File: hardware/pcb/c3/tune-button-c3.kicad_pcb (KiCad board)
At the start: 2 copper layers, 46 x 77 mm, 39 parts, among them J1 USB-C, J2 LiPo, Q1 AO3401A, SW1 MX switch, SW2 MX switch, SW3 MX switch, SW4 MX switch, SW5 RESET, SW6 BOOT, U1 ESP32-C3-WROOM-02-N4, U2 USBLC6-2SC6, U3 MCP73831-2, U4 MCP1700-3302E

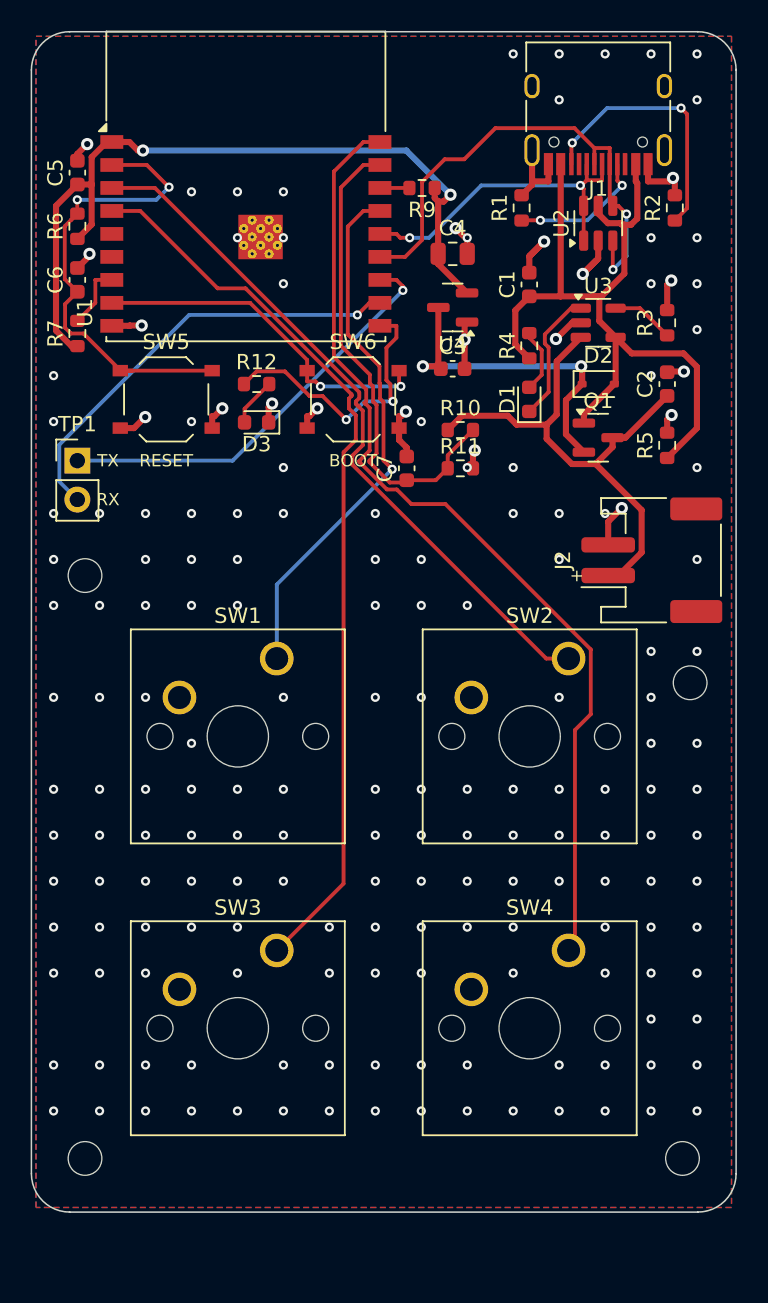
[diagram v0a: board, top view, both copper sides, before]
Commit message: PCBs: keep screw heads and labels clear of the keycaps
Mounting holes move out from under the caps (both boards 2.5 mm longer), and part labels are placed
automatically beside each part, off pads, bodies and the XIAO's outline.
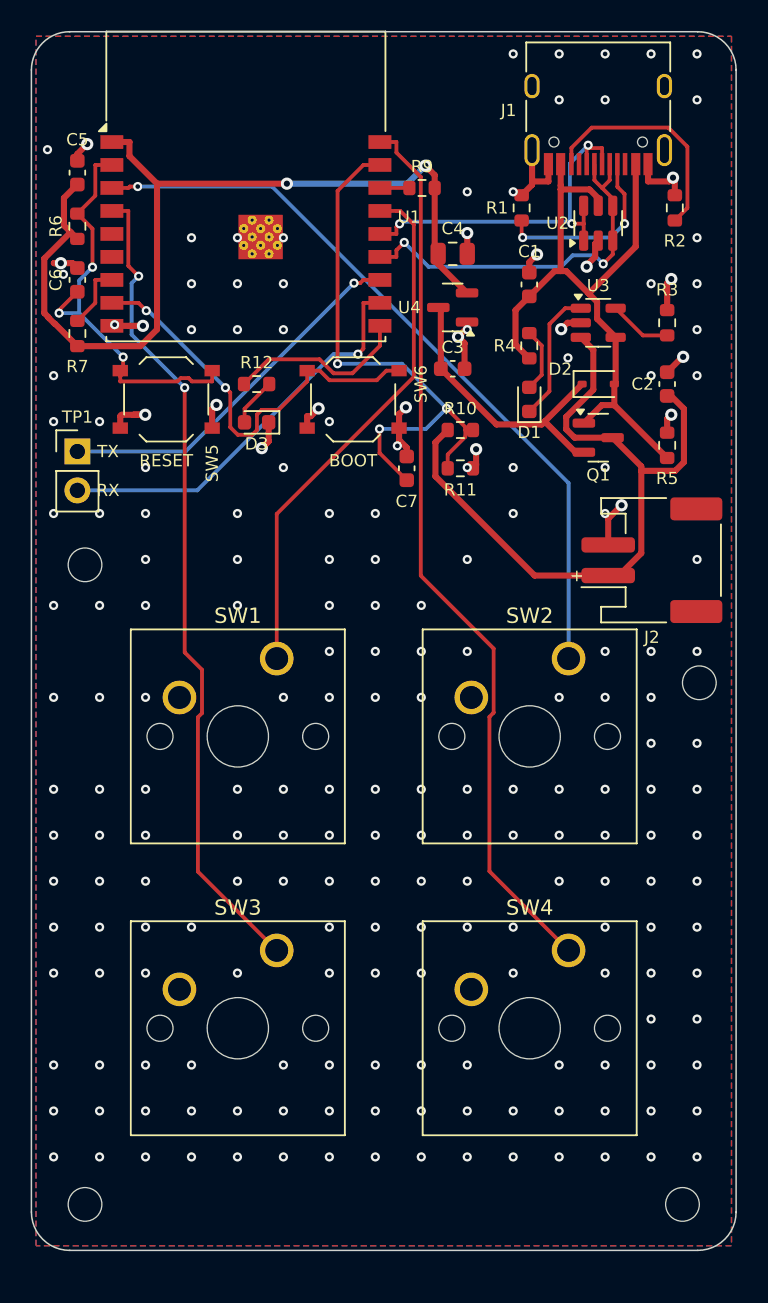
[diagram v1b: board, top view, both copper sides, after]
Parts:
- moved H1 3.00 mm to (42.5, 76.5)
- moved H2 3.00 mm to (3.50, 76.5)
- moved H3 0.70 mm to (3.50, 34.8)
- moved H4 0.60 mm to (43.6, 42.5)
- moved TP1 0.60 mm to (3.00, 27.4)
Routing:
- net VBAT: track 35.2 -> 46.7 mm
- net 3V3: track 52.6 -> 60.6 mm
- net VBUS: track 53.0 -> 45.2 mm
- net USB_DN: track 33.2 -> 25.4 mm
- net LED: track 18.3 -> 12.0 mm, vias 2 -> 0
- net VBAT_SENSE: track 31.5 -> 37.5 mm, vias 0 -> 3
- net K4: track 64.6 -> 58.7 mm
- net K3: track 59.3 -> 54.0 mm, vias 0 -> 2
- net EN: track 32.2 -> 28.1 mm, vias 2 -> 3
- net IO9: track 23.0 -> 26.9 mm
- net TXD: track 27.8 -> 24.4 mm
- net CC1: track 9.03 -> 12.2 mm
- net USB_DP: track 22.0 -> 25.0 mm, vias 2 -> 3
- net K2: track 46.6 -> 49.3 mm, vias 0 -> 1
- net VSYS: track 22.0 -> 19.3 mm, vias 2 -> 0
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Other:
- board size 46 x 77 mm -> 46 x 79.5 mm

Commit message: C3 PCB: no board under the antenna, USB-C to the bottom edge
The top-left corner is cut away under the module's antenna, as Espressif's layout guide prefers,
and USB-C moves to the middle of the bottom edge (about 70 mm from the antenna) with its ESD
part and CC resistors between the lower switches. The receptacle's face now sits 0.2 mm proud of
the edge so a plug's moulding clears the board.
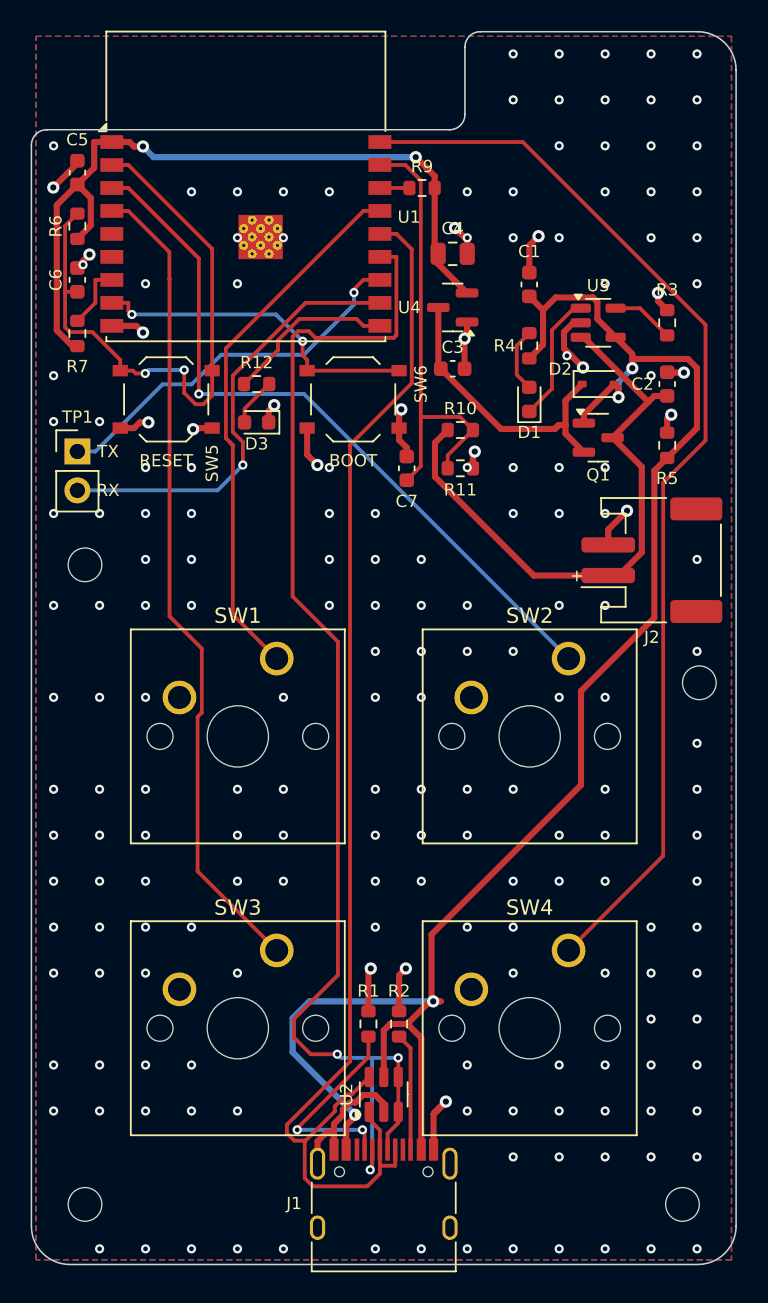
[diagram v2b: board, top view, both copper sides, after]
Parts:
- moved J1 73.8 mm to (23.0, 77.0), turned to 0 degrees
- moved U2 58.6 mm to (23.0, 69.4)
- moved R2 56.2 mm to (24.0, 64.8)
- moved R1 54.2 mm to (22.0, 64.8)
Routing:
- net VBUS: track 45.2 -> 110.0 mm, vias 0 -> 4
- net USB_DP: track 25.0 -> 85.4 mm, vias 3 -> 0
- net USB_DN: track 25.4 -> 83.9 mm, vias 2 -> 3
- net EN: track 28.1 -> 40.3 mm, vias 3 -> 2
- net K4: track 58.7 -> 70.7 mm
- net 3V3: track 60.6 -> 51.0 mm
- net GND: track 49.7 -> 57.4 mm, vias 208 -> 197
- net VBAT_SENSE: track 37.5 -> 30.0 mm, vias 3 -> 0
- net VBAT: track 46.7 -> 39.3 mm
- net CC2: track 14.9 -> 7.69 mm
- net IO9: track 26.9 -> 21.8 mm
- net RXD: track 26.6 -> 29.2 mm
- net K2: track 49.3 -> 47.7 mm
- net CC1: track 12.2 -> 13.6 mm
- net K1: track 34.6 -> 35.7 mm
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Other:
- board size 46 x 79.5 mm -> 46 x 80.5 mm

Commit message: C3 PCB: JLC Basic/Preferred parts where a drop-in exists, LCSC numbers, JLC BOM and CPL
TP4054 for MCP73831, XC6206 for MCP1700 and SRV05-4 for USBLC6-2SC6, each with the same footprint
and pinout. Every assembled part carries its LCSC number; the build writes JLC-format BOM and
placement files listing only those parts. Only the module, USB-C and JST sockets remain Extended.
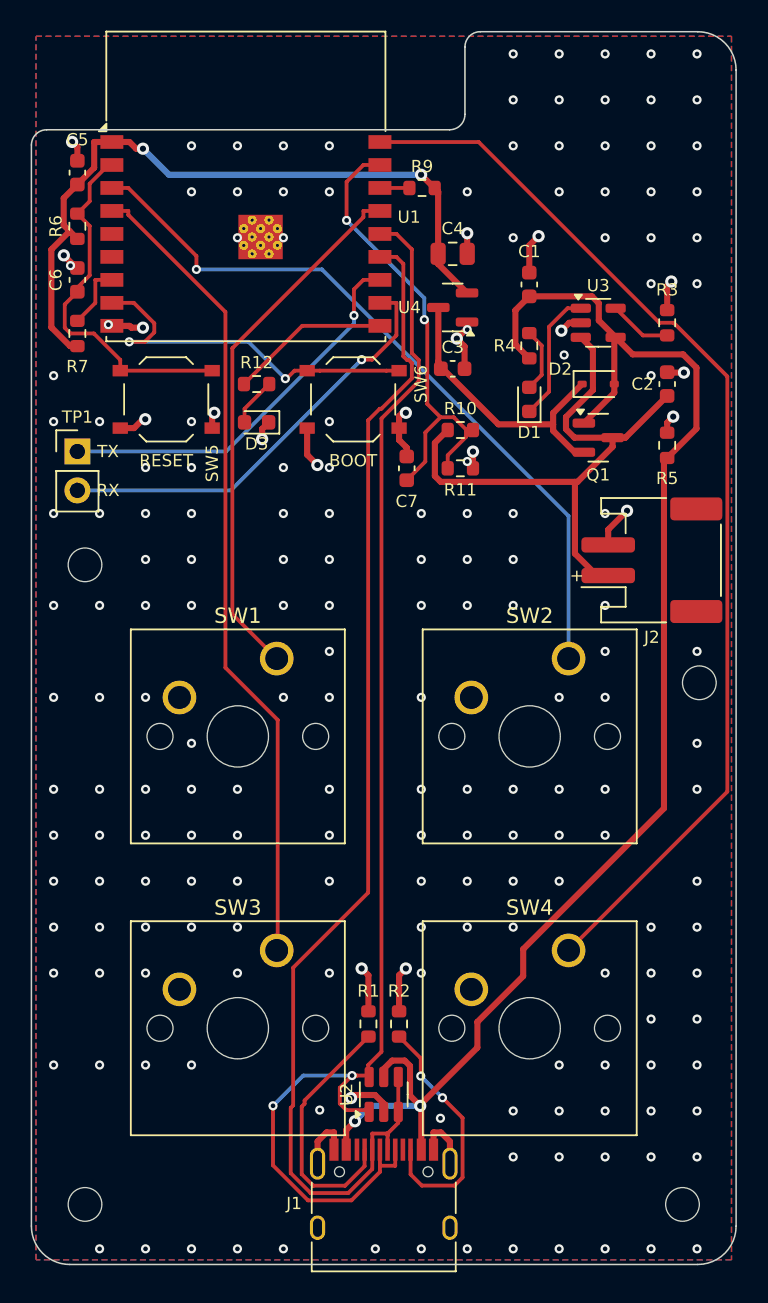
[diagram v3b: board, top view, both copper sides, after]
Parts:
- U2: value USBLC6-2SC6 -> SRV05-4
- U3: value MCP73831-2 -> TP4054
- U4: value MCP1700-3302E -> XC6206P332MR
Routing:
- net EN: track 40.3 -> 23.9 mm, vias 2 -> 0
- net VBUS: track 110.0 -> 95.6 mm, vias 4 -> 2
- net CC2: track 7.69 -> 16.4 mm, vias 0 -> 2
- net GND: track 57.4 -> 49.9 mm, vias 197 -> 199
- net USB_DN: track 83.9 -> 79.6 mm, vias 3 -> 0
- net CC1: track 13.6 -> 16.8 mm, vias 2 -> 0
- net 3V3: track 51.0 -> 48.2 mm
- net IO9: track 21.8 -> 24.6 mm
- net VBAT_SENSE: track 30.0 -> 31.0 mm, vias 0 -> 2
- net RXD: track 29.2 -> 28.2 mm
- net K2: track 47.7 -> 48.5 mm
- net LED: track 11.2 -> 10.4 mm
- net TXD: track 25.0 -> 25.7 mm
- net K1: track 35.7 -> 35.0 mm
- net USB_DP: track 85.4 -> 85.5 mm, vias 0 -> 2

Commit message: C3 PCB: switches and LEDs on the back, electronics on the front, EdgeCoil mark on the key side
The MX switches mount on the back (mirrored so K1 is still top left from the key side), and only
their leads and posts need room on the front, guarded by part-free rule areas. That lets the keys
sit behind the electronics: the board is 69.5 mm long instead of 80.5. The two LEDs move to the key
side as hand-soldered 0805s; the battery socket and UART pads sit between the key rows. The key side
carries the mark, the board name and LED labels; part labels are placed per side and kept off the
antenna notch.
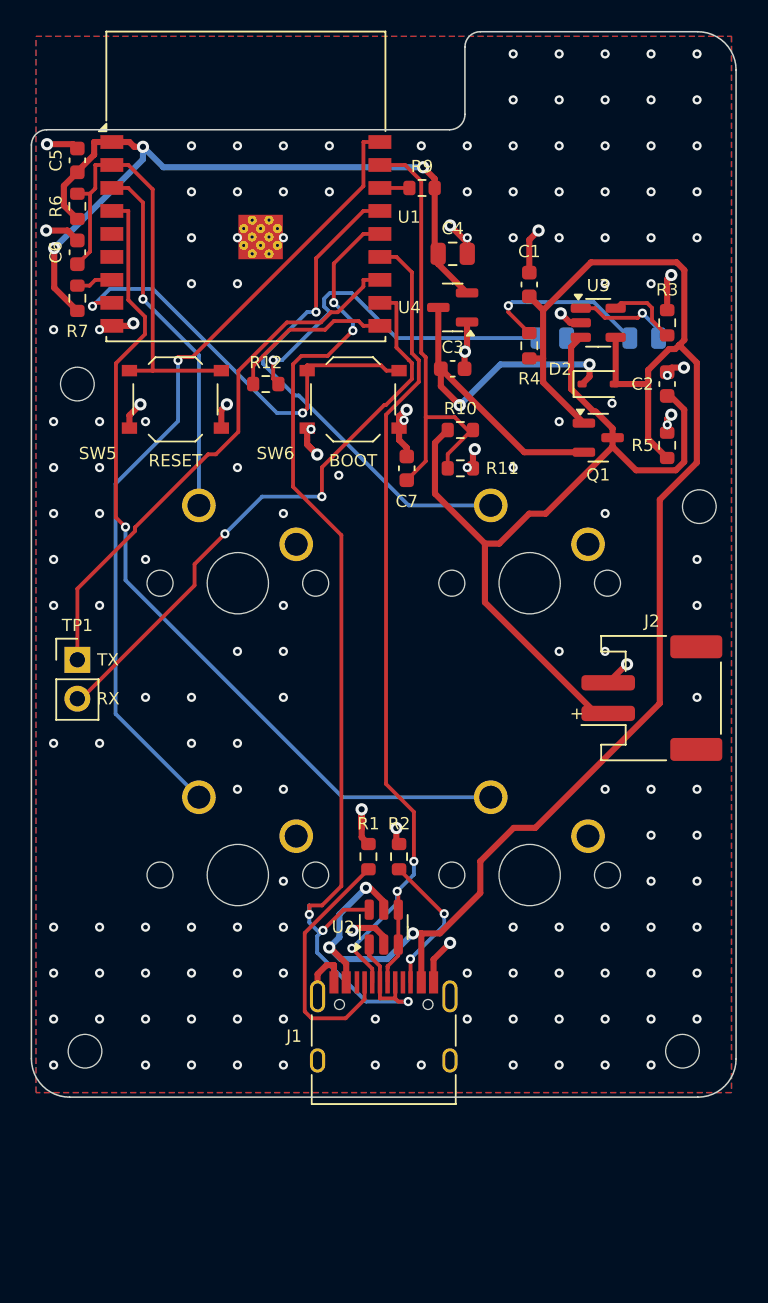
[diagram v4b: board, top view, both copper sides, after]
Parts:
- D1, D3: footprint LED_SMD:LED_0603_1608Metric -> LED_SMD:LED_0805_2012Metric; moved to B.Cu
- SW1, SW2, SW3, SW4: moved to B.Cu
- moved SW2 26.1 mm to (10.9, 30.9), turned to 180 degrees
- moved SW4 26.1 mm to (10.9, 50.0), turned to 180 degrees
- moved D3 20.1 mm to (34.0, 20.0)
- moved SW1 17.2 mm to (30.0, 30.9), turned to 180 degrees
- moved SW3 17.2 mm to (30.0, 50.0), turned to 180 degrees
- moved TP1 13.6 mm to (3.00, 41.0)
- moved H3 11.8 mm to (3.00, 23.0)
- moved H4 11.5 mm to (43.6, 31.0)
- moved J1 10.9 mm to (23.0, 66.1)
- moved U2 10.9 mm to (23.0, 58.5)
- moved R1 10.9 mm to (22.0, 53.9)
- moved R2 10.9 mm to (24.0, 53.9)
- moved H1 10.0 mm to (42.5, 66.5)
- moved H2 10.0 mm to (3.50, 66.5)
- moved J2 9.00 mm to (40.5, 43.5)
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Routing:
- net K2: track 48.5 -> 23.7 mm
- net USB_DN: track 79.6 -> 59.2 mm, vias 0 -> 3
- net LED_A: track 3.17 -> 23.0 mm, vias 0 -> 1
- net K4: track 70.8 -> 53.4 mm, vias 0 -> 1
- net VBAT: track 39.1 -> 54.0 mm
- net VBUS: track 95.6 -> 108.5 mm, vias 2 -> 3
- net USB_DP: track 85.5 -> 74.0 mm, vias 2 -> 5
- net RXD: track 28.2 -> 38.9 mm, vias 1 -> 2
- net VSYS: track 19.8 -> 29.6 mm, vias 0 -> 2
- net TXD: track 25.7 -> 35.5 mm, vias 1 -> 0
- net CHG_A: track 4.21 -> 11.3 mm, vias 0 -> 1
- net CC2: track 16.4 -> 9.54 mm
- net EN: track 23.9 -> 30.0 mm
- net IO9: track 24.6 -> 28.3 mm
- net 3V3: track 48.2 -> 51.5 mm, vias 2 -> 3
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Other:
- board size 46 x 80.5 mm -> 46 x 69.5 mm
- board text added: "CHG"
- board text added: "LED"
- board text added: "c3 · rev A"
- board text added: "edgecoil"
- board text added: "tune-button"
- board text removed: "tune-button c3 edgecoil rev A"

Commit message: pcb: MCP1700 regulator, edgecoil.dev on the silkscreen, mark under its own licence
The EdgeCoil mark, name and URL are all rights reserved and outside CERN-OHL-S; derivatives must
remove them. The C3 board's regulator goes back to the 250 mA MCP1700 (C39051, Extended).
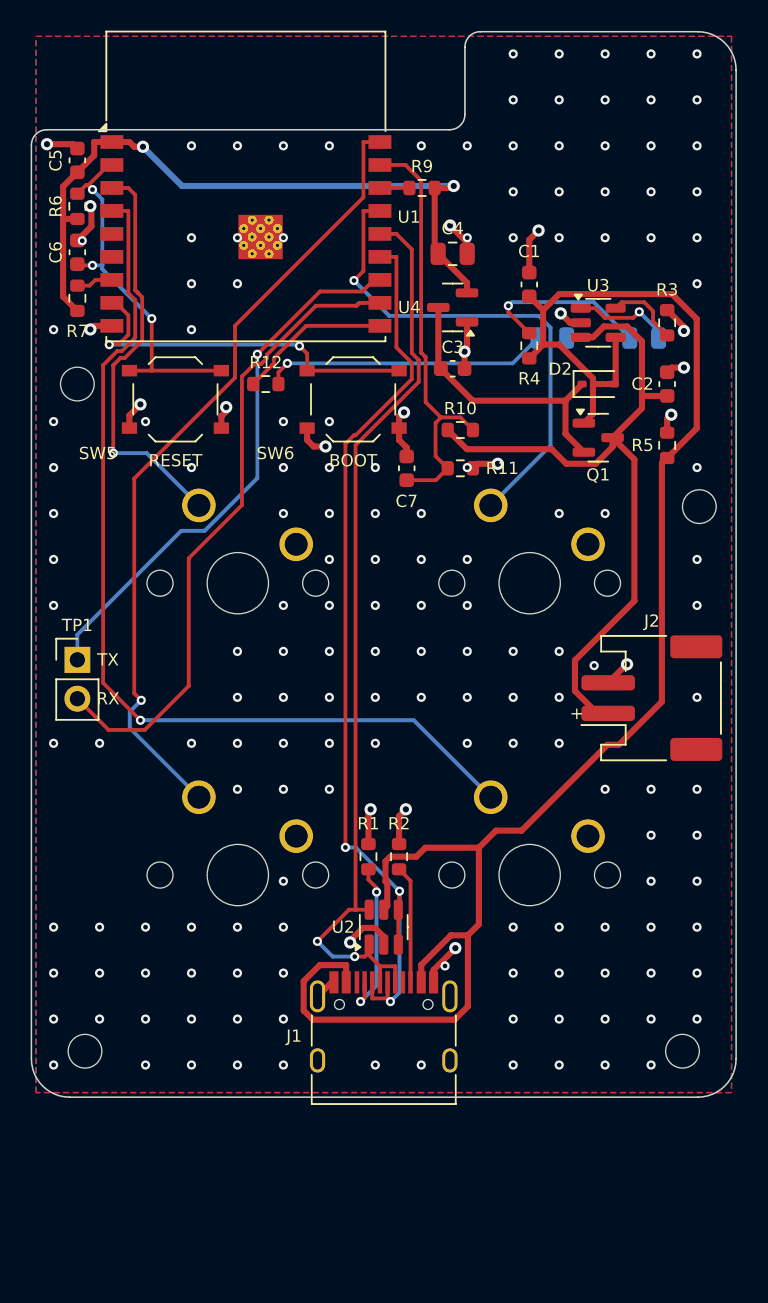
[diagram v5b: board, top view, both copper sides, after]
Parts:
- U4: value XC6206P332MR -> MCP1700-3.3
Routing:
- net USB_DP: track 74.0 -> 60.4 mm, vias 5 -> 2
- net VSYS: track 29.6 -> 18.5 mm, vias 2 -> 0
- net VBAT: track 54.0 -> 47.7 mm
- net GND: track 51.6 -> 45.8 mm, vias 161 -> 176
- net EN: track 30.0 -> 24.5 mm, vias 0 -> 3
- net CC1: track 16.7 -> 11.2 mm, vias 0 -> 2
- net K3: track 56.4 -> 61.5 mm
- net 3V3: track 51.5 -> 46.9 mm, vias 3 -> 2
- net LED_A: track 23.0 -> 18.6 mm
- net VBUS: track 108.5 -> 112.6 mm, vias 3 -> 0
- net IO9: track 28.3 -> 24.5 mm
- net RXD: track 38.9 -> 42.3 mm, vias 2 -> 0
- net K2: track 23.7 -> 27.0 mm
- net CC2: track 9.54 -> 7.69 mm, vias 2 -> 0
- net USB_DN: track 59.2 -> 61.0 mm
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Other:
- board text added: "edgecoil.dev"
- board text removed: "edgecoil"

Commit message: pcb: DFM fixes from audit; artwork clear of drilled holes
- fab_jlc.py: per-part CPL rotation and origin corrections (MCP1700, AO3401A, SRV05-4, TP4054,
  USB-C), checked against JLC's own footprints; the SRV05-4 one would have shorted VBUS.
- Paste on the USB-C shell slots; thermal spokes on all pour pads; copper 0.3 mm from the edge.
- Silkscreen text 1.0 mm / 0.15 mm; switch-pin keep-outs 2.5 mm, R10/R11/C7 moved for iron room.
- Via-free rule areas under back artwork, honoured by the stitcher; the build refuses a footprint
  hole under artwork. C3 mark moved off the module's ground vias; XIAO text off SW4's pins.
- No drill maps or back paste in the gerber zip.
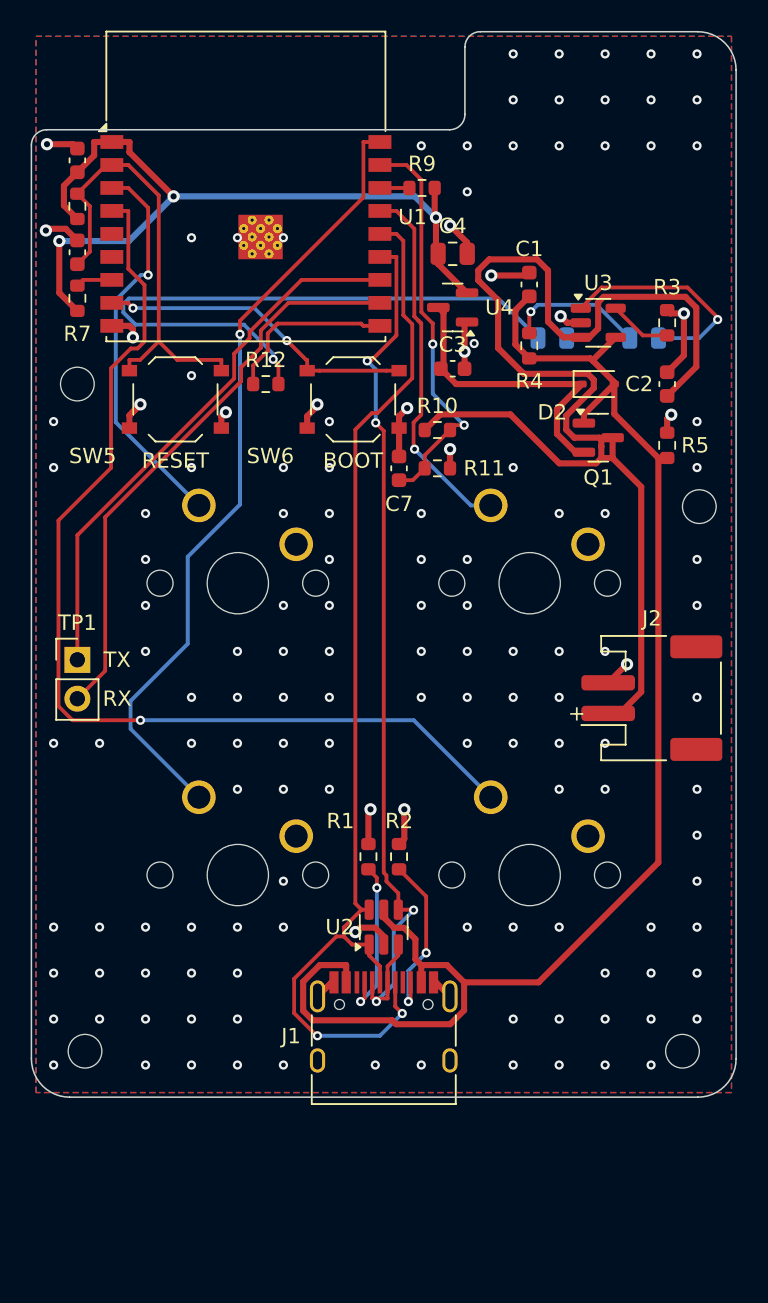
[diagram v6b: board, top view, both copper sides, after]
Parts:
- moved R10 1.50 mm to (26.5, 26.0)
- moved R11 1.50 mm to (26.5, 28.5)
- moved C7 0.50 mm to (24.0, 28.5)
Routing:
- net VBAT: track 47.7 -> 82.3 mm
- net LED_A: track 18.6 -> 41.8 mm
- net VBUS: track 112.6 -> 94.3 mm
- net USB_DP: track 60.4 -> 72.0 mm
- net K1: track 33.2 -> 24.3 mm
- net STAT: track 6.47 -> 14.8 mm
- net EN: track 24.5 -> 30.1 mm, vias 3 -> 0
- net K3: track 61.5 -> 67.1 mm
- net 3V3: track 46.9 -> 52.4 mm, vias 2 -> 3
- net RXD: track 42.3 -> 37.5 mm
- net CC2: track 7.69 -> 11.2 mm, vias 0 -> 2
- net IO9: track 24.5 -> 21.0 mm
- net CHG_A: track 11.3 -> 8.99 mm
- net VBAT_SENSE: track 28.4 -> 26.5 mm, vias 0 -> 2
- net VSYS: track 18.5 -> 20.0 mm
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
